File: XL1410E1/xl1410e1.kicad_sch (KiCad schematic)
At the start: 18 parts, among them J1 Conn_01x04, J2 Conn_01x04, J3 Conn_01x04, J4 Conn_01x04, U1 XL1410

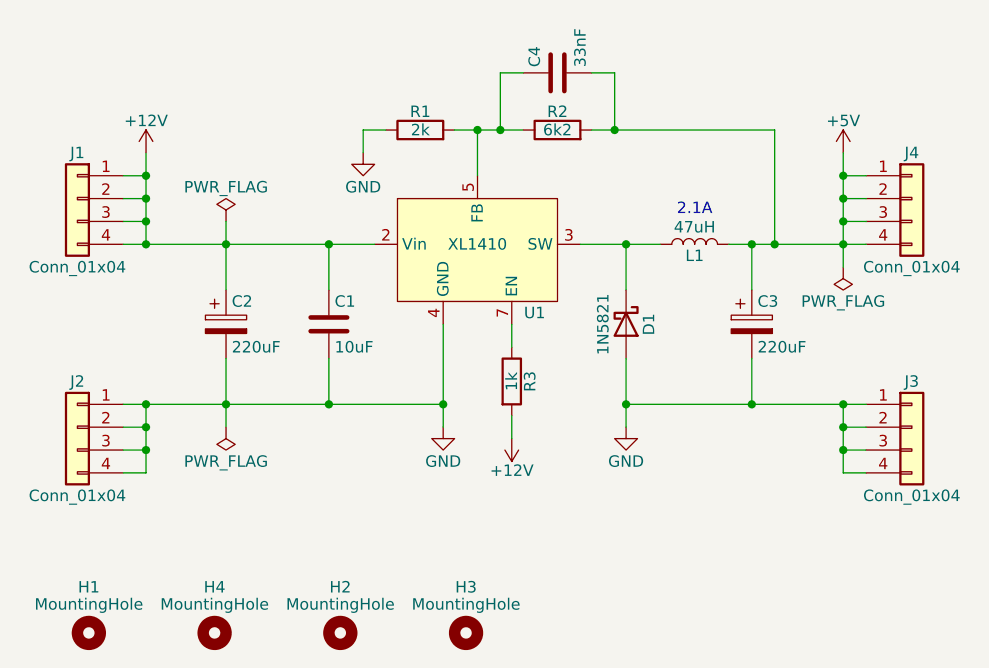
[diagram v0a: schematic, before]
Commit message: change fbk resistor values
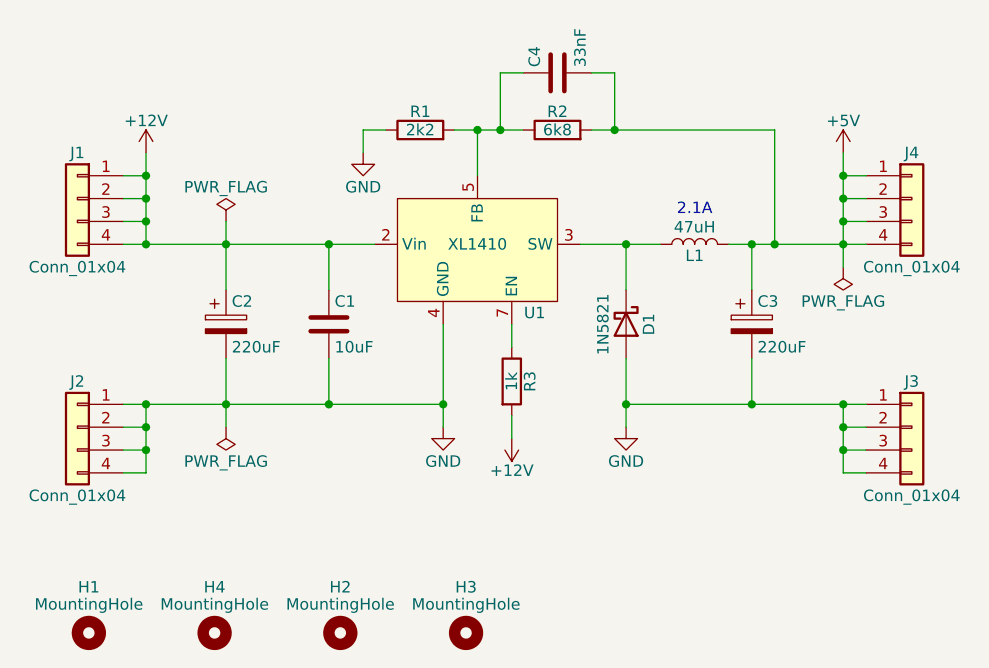
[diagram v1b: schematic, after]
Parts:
- R1: value 2k -> 2k2
- R2: value 6k2 -> 6k8
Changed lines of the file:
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@@
 			)
 		)
-		(property "Value" "2k"
+		(property "Value" "2k2"
 			(at 129.54 80.01 90)
 			(effects
@@
 			)
 		)
-		(property "Value" "6k2"
+		(property "Value" "6k8"
 			(at 144.78 80.01 90)
 			(effects
